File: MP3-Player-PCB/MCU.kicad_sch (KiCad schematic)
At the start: 19 parts, among them J101 Conn_ARM_SWD_TagConnect_TC2030, U101 STM32F411CEUx, Y101 8MHz

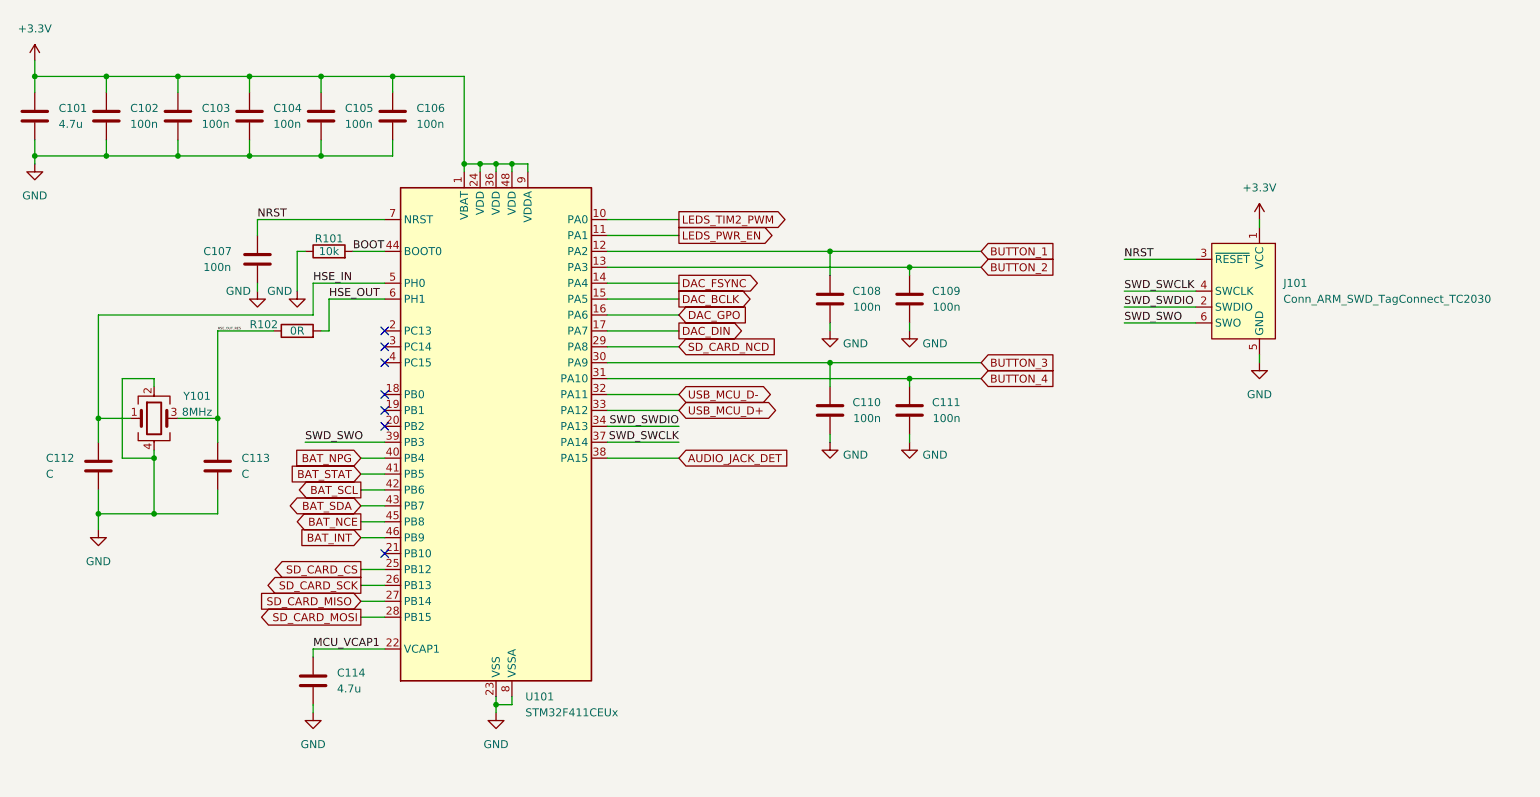
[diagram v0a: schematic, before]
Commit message: Added adc pin and voltage divider to read battery voltage. Also added charging status leds, and assigned some footprints
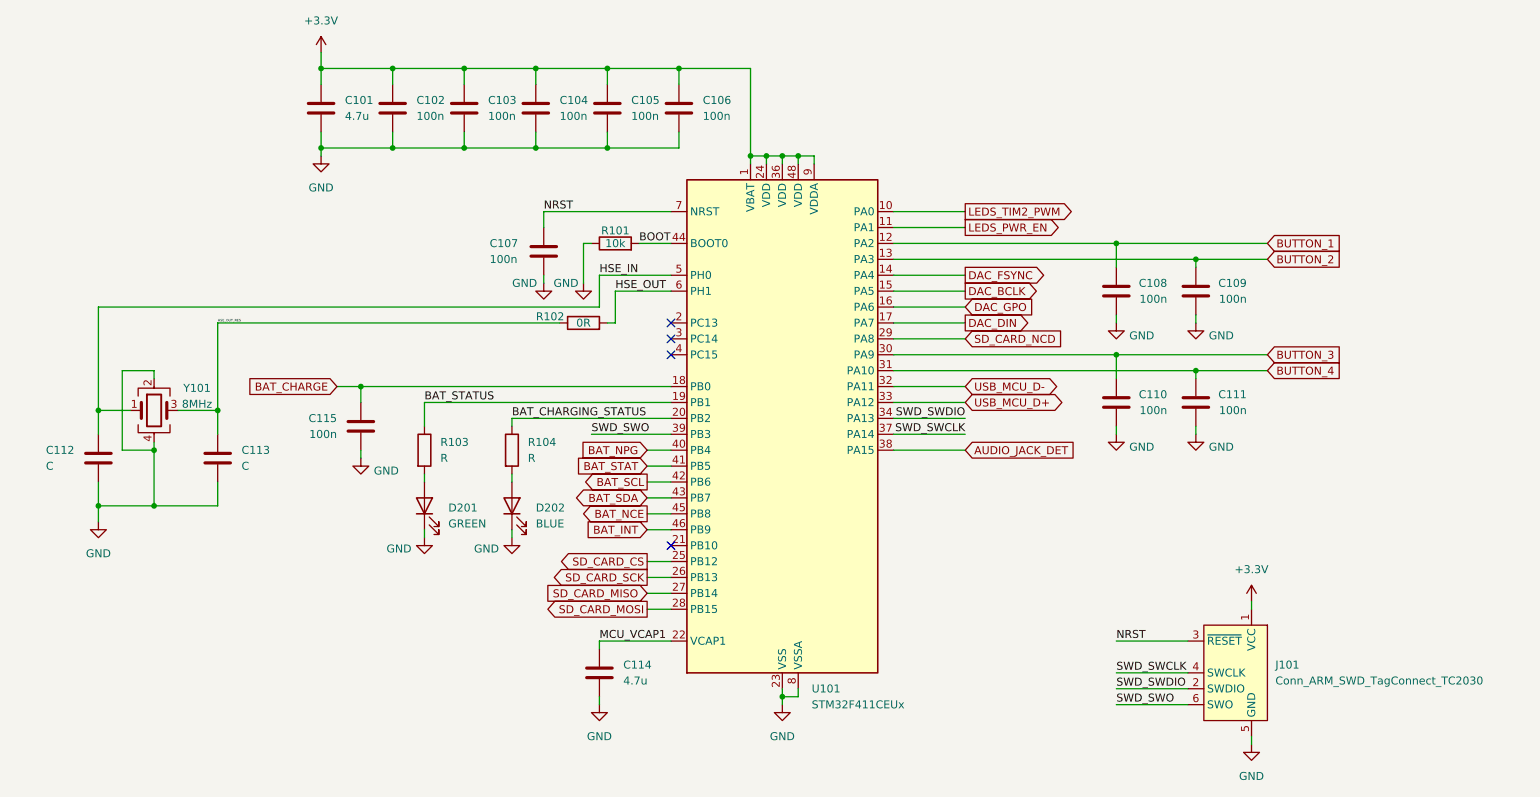
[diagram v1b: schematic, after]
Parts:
- added C115: 100n, Capacitor_SMD:C_0603_1608Metric, symbol Device:C
- added D201: GREEN, symbol Device:LED
- added D202: BLUE, symbol Device:LED
- added R103, R104: R, symbol Device:R
- C101, C114: footprint (none) -> Capacitor_SMD:C_0805_2012Metric
- C102, C103, C104, C105, C106, C107, C108, C109, C110, C111, C112, C113: footprint (none) -> Capacitor_SMD:C_0603_1608Metric
- Y101: footprint (none) -> Crystal:Crystal_SMD_3225-4Pin_3.2x2.5mm
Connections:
- net GND: now also C115.2, D201.1 (K), D202.1 (K)
- net BAT_CHARGE: now reaches U101.18 (PB0)
- net BAT_CHARGE: now also C115.1
- net BAT_STATUS: now reaches U101.19 (PB1)
- net BAT_STATUS: now also R103.1
- net BAT_CHARGING_STATUS: now reaches U101.20 (PB2)
- net BAT_CHARGING_STATUS: now also R104.1
- new net: D202.2 (A), R104.2
- new net: D201.2 (A), R103.2
- no-connect marks 7 -> 4
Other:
- moved on the sheet: C101, C102, C103, C104, C105, C106, C107, C108, C109, C110, C111, C112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

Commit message: Assigned all footprints
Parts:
- D201, D202: footprint (none) -> LED_SMD:LED_0402_1005Metric
- R101, R103, R104: footprint (none) -> Resistor_SMD:R_0402_1005Metric
- R102: footprint (none) -> Resistor_SMD:R_0603_1608Metric
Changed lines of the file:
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@@
 			)
 		)
-		(property "Footprint" ""
+		(property "Footprint" "Resistor_SMD:R_0402_1005Metric"
 			(at 111.252 99.06 90)
 			(effects
@@
 			)
 		)
-		(property "Footprint" ""
+		(property "Footprint" "LED_SMD:LED_0402_1005Metric"
 			(at 99.06 107.95 0)
 			(effects
@@
 			)
 		)
-		(property "Footprint" ""
+		(property "Footprint" "Resistor_SMD:R_0402_1005Metric"
 			(at 129.54 67.818 90)
 			(effects
@@
 			)
 		)
-		(property "Footprint" ""
+		(property "Footprint" "Resistor_SMD:R_0402_1005Metric"
 			(at 97.282 99.06 90)
 			(effects
@@
 			)
 		)
-		(property "Footprint" ""
+		(property "Footprint" "Resistor_SMD:R_0603_1608Metric"
 			(at 124.46 80.518 90)
 			(effects
@@
 			)
 		)
-		(property "Footprint" ""
+		(property "Footprint" "LED_SMD:LED_0402_1005Metric"
 			(at 113.03 107.95 0)
 			(effects

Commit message: Fixed all ERC errors
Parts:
- renumbered C115 to C112, C112 to C113, C113 to C114, C114 to C115, D201 to D101, D202 to D102
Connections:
- net SD_CARD_CS renamed SD_CARD_NCS

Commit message: Much better initial layout
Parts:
- C101, C115: footprint Capacitor_SMD:C_0805_2012Metric -> Capacitor_SMD:C_0603_1608Metric
- C102, C103, C104, C105, C106, C107, C108, C109, C110, C111, C112: footprint Capacitor_SMD:C_0603_1608Metric -> Capacitor_SMD:C_0402_1005Metric
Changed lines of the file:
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@@
 			)
 		)
-		(property "Footprint" "Capacitor_SMD:C_0603_1608Metric"
+		(property "Footprint" "Capacitor_SMD:C_0402_1005Metric"
 			(at 106.3752 48.26 0)
 			(effects
@@
 			)
 		)
-		(property "Footprint" "Capacitor_SMD:C_0603_1608Metric"
+		(property "Footprint" "Capacitor_SMD:C_0402_1005Metric"
 			(at 87.9348 99.06 0)
 			(effects
@@
 			)
 		)
-		(property "Footprint" "Capacitor_SMD:C_0603_1608Metric"
+		(property "Footprint" "Capacitor_SMD:C_0402_1005Metric"
 			(at 221.2848 95.25 0)
 			(effects
@@
 			)
 		)
-		(property "Footprint" "Capacitor_SMD:C_0603_1608Metric"
+		(property "Footprint" "Capacitor_SMD:C_0402_1005Metric"
 			(at 140.6652 48.26 0)
 			(effects
@@
 			)
 		)
-		(property "Footprint" "Capacitor_SMD:C_0603_1608Metric"
+		(property "Footprint" "Capacitor_SMD:C_0402_1005Metric"
 			(at 208.5848 95.25 0)
 			(effects
@@
 			)
 		)
-		(property "Footprint" "Capacitor_SMD:C_0603_1608Metric"
+		(property "Footprint" "Capacitor_SMD:C_0402_1005Metric"
 			(at 129.2352 48.26 0)
 			(effects
@@
 			)
 		)
-		(property "Footprint" "Capacitor_SMD:C_0603_1608Metric"
+		(property "Footprint" "Capacitor_SMD:C_0402_1005Metric"
 			(at 208.5848 77.47 0)
 			(effects
@@
 			)
 		)
-		(property "Footprint" "Capacitor_SMD:C_0603_1608Metric"
+		(property "Footprint" "Capacitor_SMD:C_0402_1005Metric"
 			(at 94.9452 48.26 0)
 			(effects
@@
 			)
 		)
-		(property "Footprint" "Capacitor_SMD:C_0805_2012Metric"
+		(property "Footprint" "Capacitor_SMD:C_0603_1608Metric"
 			(at 127.9652 138.43 0)
 			(effects
@@
 			)
 		)
-		(property "Footprint" "Capacitor_SMD:C_0603_1608Metric"
+		(property "Footprint" "Capacitor_SMD:C_0402_1005Metric"
 			(at 117.8052 48.26 0)
 			(effects
@@
 			)
 		)
-		(property "Footprint" "Capacitor_SMD:C_0805_2012Metric"
+		(property "Footprint" "Capacitor_SMD:C_0603_1608Metric"
 			(at 83.5152 48.26 0)
 			(effects
@@
 			)
 		)
-		(property "Footprint" "Capacitor_SMD:C_0603_1608Metric"
+		(property "Footprint" "Capacitor_SMD:C_0402_1005Metric"
 			(at 119.0752 71.12 0)
 			(effects
@@
 			)
 		)
-		(property "Footprint" "Capacitor_SMD:C_0603_1608Metric"
+		(property "Footprint" "Capacitor_SMD:C_0402_1005Metric"
 			(at 221.2848 77.47 0)
 			(effects

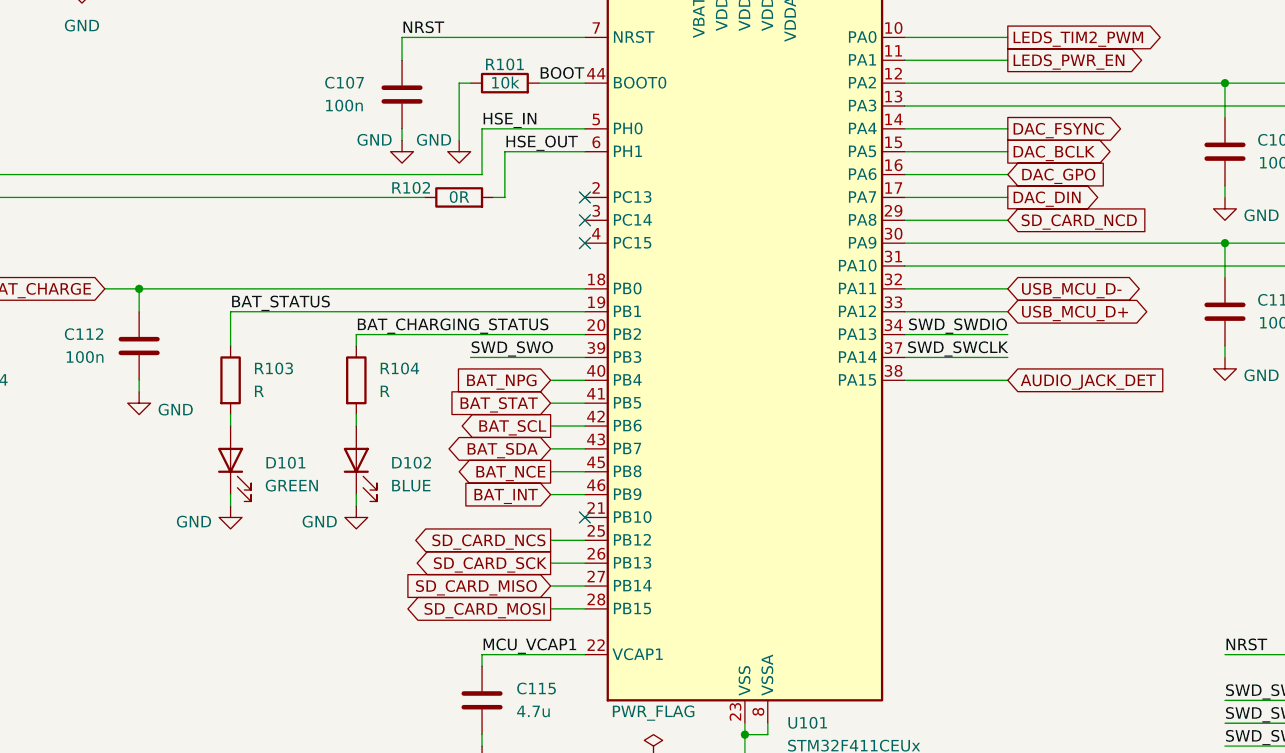
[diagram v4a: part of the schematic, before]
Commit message: Routing more mcu signals
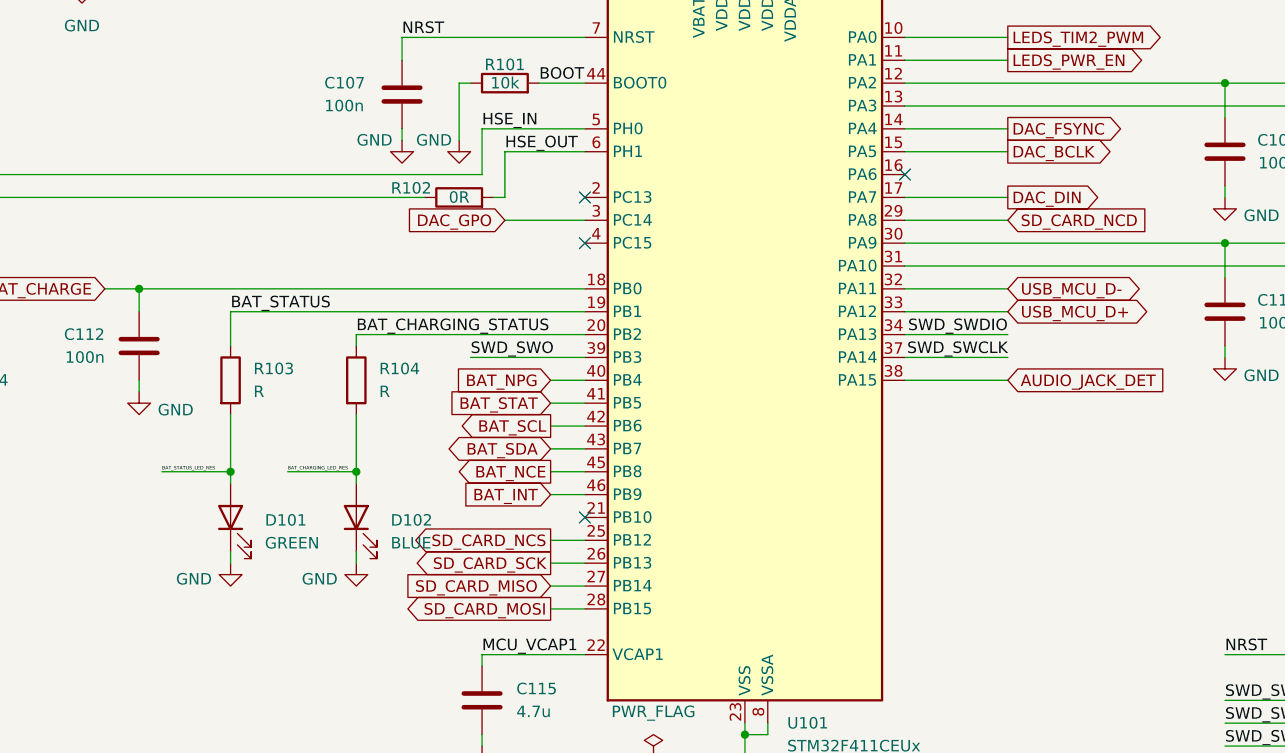
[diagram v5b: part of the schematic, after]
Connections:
- net DAC_GPO: now also U101.3 (PC14); no longer U101.16 (PA6)
- net BAT_CHARGING_LED_RES: now reaches D102.2 (A), R104.2
- net BAT_STATUS_LED_RES: now reaches D101.2 (A), R103.2
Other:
- moved on the sheet: D101, D102
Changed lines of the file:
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@@
 	)
 	(junction
+		(at 113.03 109.22)
+		(diameter 0)
+		(color 0 0 0 0)
+	)
+	(junction
+		(at 99.06 109.22)
+		(diameter 0)
+		(color 0 0 0 0)
+	)
+	(junction
 		(at 82.55 38.1)
 		(diameter 0)
@@
 	)
 	(no_connect
-		(at 138.43 81.28)
+		(at 173.99 76.2)
 	)
 	(no_connect
@@
 	(wire
 		(pts
+			(xy 129.54 81.28) (xy 138.43 81.28)
+		)
+		(stroke
+			(width 0)
+			(type default)
+		)
+	)
+	(wire
+		(pts
 			(xy 55.88 87.63) (xy 55.88 86.36)
 		)
@@
 	(wire
 		(pts
+			(xy 99.06 109.22) (xy 99.06 102.87)
+		)
+		(stroke
+			(width 0)
+			(type default)
+		)
+	)
+	(wire
+		(pts
 			(xy 50.8 99.06) (xy 55.88 99.06)
 		)
@@
 	(wire
 		(pts
-			(xy 113.03 111.76) (xy 113.03 113.03)
+			(xy 113.03 118.11) (xy 113.03 119.38)
 		)
 		(stroke
@@
 	(wire
 		(pts
-			(xy 99.06 111.76) (xy 99.06 113.03)
+			(xy 99.06 118.11) (xy 99.06 119.38)
 		)
 		(stroke
@@
 	(wire
 		(pts
+			(xy 113.03 109.22) (xy 113.03 110.49)
+		)
+		(stroke
+			(width 0)
+			(type default)
+		)
+	)
+	(wire
+		(pts
 			(xy 127 71.12) (xy 138.43 71.12)
 		)
@@
 	(wire
 		(pts
+			(xy 105.41 109.22) (xy 113.03 109.22)
+		)
+		(stroke
+			(width 0)
+			(type default)
+		)
+	)
+	(wire
+		(pts
 			(xy 59.69 92.71) (xy 66.04 92.71)
 		)
@@
 	(wire
 		(pts
-			(xy 113.03 102.87) (xy 113.03 104.14)
+			(xy 113.03 102.87) (xy 113.03 109.22)
 		)
 		(stroke
@@
 	(wire
 		(pts
-			(xy 99.06 104.14) (xy 99.06 102.87)
+			(xy 99.06 110.49) (xy 99.06 109.22)
 		)
 		(stroke
@@
 	(wire
 		(pts
-			(xy 173.99 76.2) (xy 185.42 76.2)
+			(xy 209.55 129.54) (xy 220.98 129.54)
 		)
 		(stroke
@@
 	(wire
 		(pts
-			(xy 209.55 129.54) (xy 220.98 129.54)
+			(xy 209.55 83.82) (xy 209.55 87.63)
 		)
 		(stroke
@@
 	(wire
 		(pts
-			(xy 209.55 83.82) (xy 209.55 87.63)
+			(xy 222.25 77.47) (xy 222.25 78.74)
 		)
 		(stroke
@@
 	(wire
 		(pts
-			(xy 222.25 77.47) (xy 222.25 78.74)
+			(xy 134.62 116.84) (xy 138.43 116.84)
 		)
 		(stroke
@@
 	(wire
 		(pts
-			(xy 134.62 116.84) (xy 138.43 116.84)
+			(xy 125.73 96.52) (xy 138.43 96.52)
 		)
 		(stroke
@@
 	(wire
 		(pts
-			(xy 125.73 96.52) (xy 138.43 96.52)
+			(xy 91.44 109.22) (xy 99.06 109.22)
 		)
 		(stroke
@@
 		)
 	)
+	(label "BAT_CHARGING_LED_RES"
+		(at 105.41 109.22 0)
+		(effects
+			(font
+				(size 0.381 0.381)
+			)
+			(justify left bottom)
+		)
+	)
+	(label "BAT_STATUS_LED_RES"
+		(at 91.44 109.22 0)
+		(effects
+			(font
+				(size 0.381 0.381)
+			)
+			(justify left bottom)
+		)
+	)
 	(label "HSE_OUT"
 		(at 129.54 73.66 0)
@@
 		)
 	)
-	(global_label "DAC_GPO"
+	(global_label "BUTTON_4"
 		(shape input)
-		(at 185.42 76.2 0)
+		(at 233.68 86.36 0)
 		(fields_autoplaced yes)
 		(effects
@@
 		)
 		(property "Intersheetrefs" "${INTERSHEET_REFS}"
-			(at 196.8719 76.2 0)
+			(at 246.039 86.36 0)
 			(effects
 				(font
@@
 		)
 	)
-	(global_label "BUTTON_4"
+	(global_label "SD_CARD_NCD"
 		(shape input)
-		(at 233.68 86.36 0)
+		(at 185.42 81.28 0)
 		(fields_autoplaced yes)
 		(effects
@@
 		)
 		(property "Intersheetrefs" "${INTERSHEET_REFS}"
-			(at 246.039 86.36 0)
+			(at 201.589 81.28 0)
 			(effects
 				(font
@@
 		)
 	)
-	(global_label "SD_CARD_NCD"
-		(shape input)
-		(at 185.42 81.28 0)
+	(global_label "DAC_DIN"
+		(shape output)
+		(at 185.42 78.74 0)
 		(fields_autoplaced yes)
 		(effects
@@
 		)
 		(property "Intersheetrefs" "${INTERSHEET_REFS}"
-			(at 201.589 81.28 0)
+			(at 196.2067 78.74 0)
 			(effects
 				(font
@@
 		)
 	)
-	(global_label "DAC_DIN"
-		(shape output)
-		(at 185.42 78.74 0)
+	(global_label "DAC_GPO"
+		(shape input)
+		(at 129.54 81.28 180)
 		(fields_autoplaced yes)
 		(effects
@@
 				(size 1.27 1.27)
 			)
-			(justify left)
+			(justify right)
 		)
 		(property "Intersheetrefs" "${INTERSHEET_REFS}"
-			(at 196.2067 78.74 0)
+			(at 118.0881 81.28 0)
 			(effects
 				(font
 					(size 1.27 1.27)
 				)
-				(justify left)
+				(justify right)
 				(hide yes)
 			)
@@
 	(symbol
 		(lib_id "power:GND")
-		(at 99.06 113.03 0)
+		(at 99.06 119.38 0)
 		(unit 1)
 		(exclude_from_sim no)
@@
 		(dnp no)
 		(property "Reference" "#PWR0111"
-			(at 99.06 119.38 0)
+			(at 99.06 125.73 0)
 			(effects
 				(font
@@
 		)
 		(property "Value" "GND"
-			(at 94.996 114.808 0)
+			(at 94.996 121.158 0)
 			(effects
 				(font
@@
 		)
 		(property "Footprint" ""
-			(at 99.06 113.03 0)
+			(at 99.06 119.38 0)
 			(effects
 				(font
@@
 		)
 		(property "Datasheet" ""
-			(at 99.06 113.03 0)
+			(at 99.06 119.38 0)
 			(effects
 				(font
@@
 		)
 		(property "Description" "Power symbol creates a global label with name \"GND\" , ground"
-			(at 99.06 113.03 0)
+			(at 99.06 119.38 0)
 			(effects
 				(font
@@
 	(symbol
 		(lib_id "Device:LED")
-		(at 99.06 107.95 90)
+		(at 99.06 114.3 90)
 		(unit 1)
 		(exclude_from_sim no)
@@
 		(fields_autoplaced yes)
 		(property "Reference" "D101"
-			(at 102.87 108.2674 90)
+			(at 102.87 114.6174 90)
 			(effects
 				(font
@@
 		)
 		(property "Value" "GREEN"
-			(at 102.87 110.8074 90)
+			(at 102.87 117.1574 90)
 			(effects
 				(font
@@
 		)
 		(property "Footprint" "LED_SMD:LED_0402_1005Metric"
-			(at 99.06 107.95 0)
+			(at 99.06 114.3 0)
 			(effects
 				(font
@@
 		)
 		(property "Datasheet" "~"
-			(at 99.06 107.95 0)
+			(at 99.06 114.3 0)
 			(effects
 				(font
@@
 		)
 		(property "Description" "Light emitting diode"
-			(at 99.06 107.95 0)
+			(at 99.06 114.3 0)
 			(effects
 				(font
@@
 		)
 		(property "Sim.Pins" "1=K 2=A"
-			(at 99.06 107.95 0)
+			(at 99.06 114.3 0)
 			(effects
 				(font
@@
 	(symbol
 		(lib_id "power:GND")
-		(at 113.03 113.03 0)
+		(at 113.03 119.38 0)
 		(unit 1)
 		(exclude_from_sim no)
@@
 		(dnp no)
 		(property "Reference" "#PWR0112"
-			(at 113.03 119.38 0)
+			(at 113.03 125.73 0)
 			(effects
 				(font
@@
 		)
 		(property "Value" "GND"
-			(at 108.966 114.808 0)
+			(at 108.966 121.158 0)
 			(effects
 				(font
@@
 		)
 		(property "Footprint" ""
-			(at 113.03 113.03 0)
+			(at 113.03 119.38 0)
 			(effects
 				(font
@@
 		)
 		(property "Datasheet" ""
-			(at 113.03 113.03 0)
+			(at 113.03 119.38 0)
 			(effects
 				(font
@@
 		)
 		(property "Description" "Power symbol creates a global label with name \"GND\" , ground"
-			(at 113.03 113.03 0)
+			(at 113.03 119.38 0)
 			(effects
 				(font
@@
 	(symbol
 		(lib_id "Device:LED")
-		(at 113.03 107.95 90)
+		(at 113.03 114.3 90)
 		(unit 1)
 		(exclude_from_sim no)
@@
 		(fields_autoplaced yes)
 		(property "Reference" "D102"
-			(at 116.84 108.2674 90)
+			(at 116.84 114.6174 90)
 			(effects
 				(font
@@
 		)
 		(property "Value" "BLUE"
-			(at 116.84 110.8074 90)
+			(at 116.84 117.1574 90)
 			(effects
 				(font
@@
 		)
 		(property "Footprint" "LED_SMD:LED_0402_1005Metric"
-			(at 113.03 107.95 0)
+			(at 113.03 114.3 0)
 			(effects
 				(font
@@
 		)
 		(property "Datasheet" "~"
-			(at 113.03 107.95 0)
+			(at 113.03 114.3 0)
 			(effects
 				(font
@@
 		)
 		(property "Description" "Light emitting diode"
-			(at 113.03 107.95 0)
+			(at 113.03 114.3 0)
 			(effects
 				(font
@@
 		)
 		(property "Sim.Pins" "1=K 2=A"
-			(at 113.03 107.95 0)
+			(at 113.03 114.3 0)
 			(effects
 				(font
